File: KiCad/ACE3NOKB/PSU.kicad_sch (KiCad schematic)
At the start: 34 parts, among them U301 74AHCT1G08

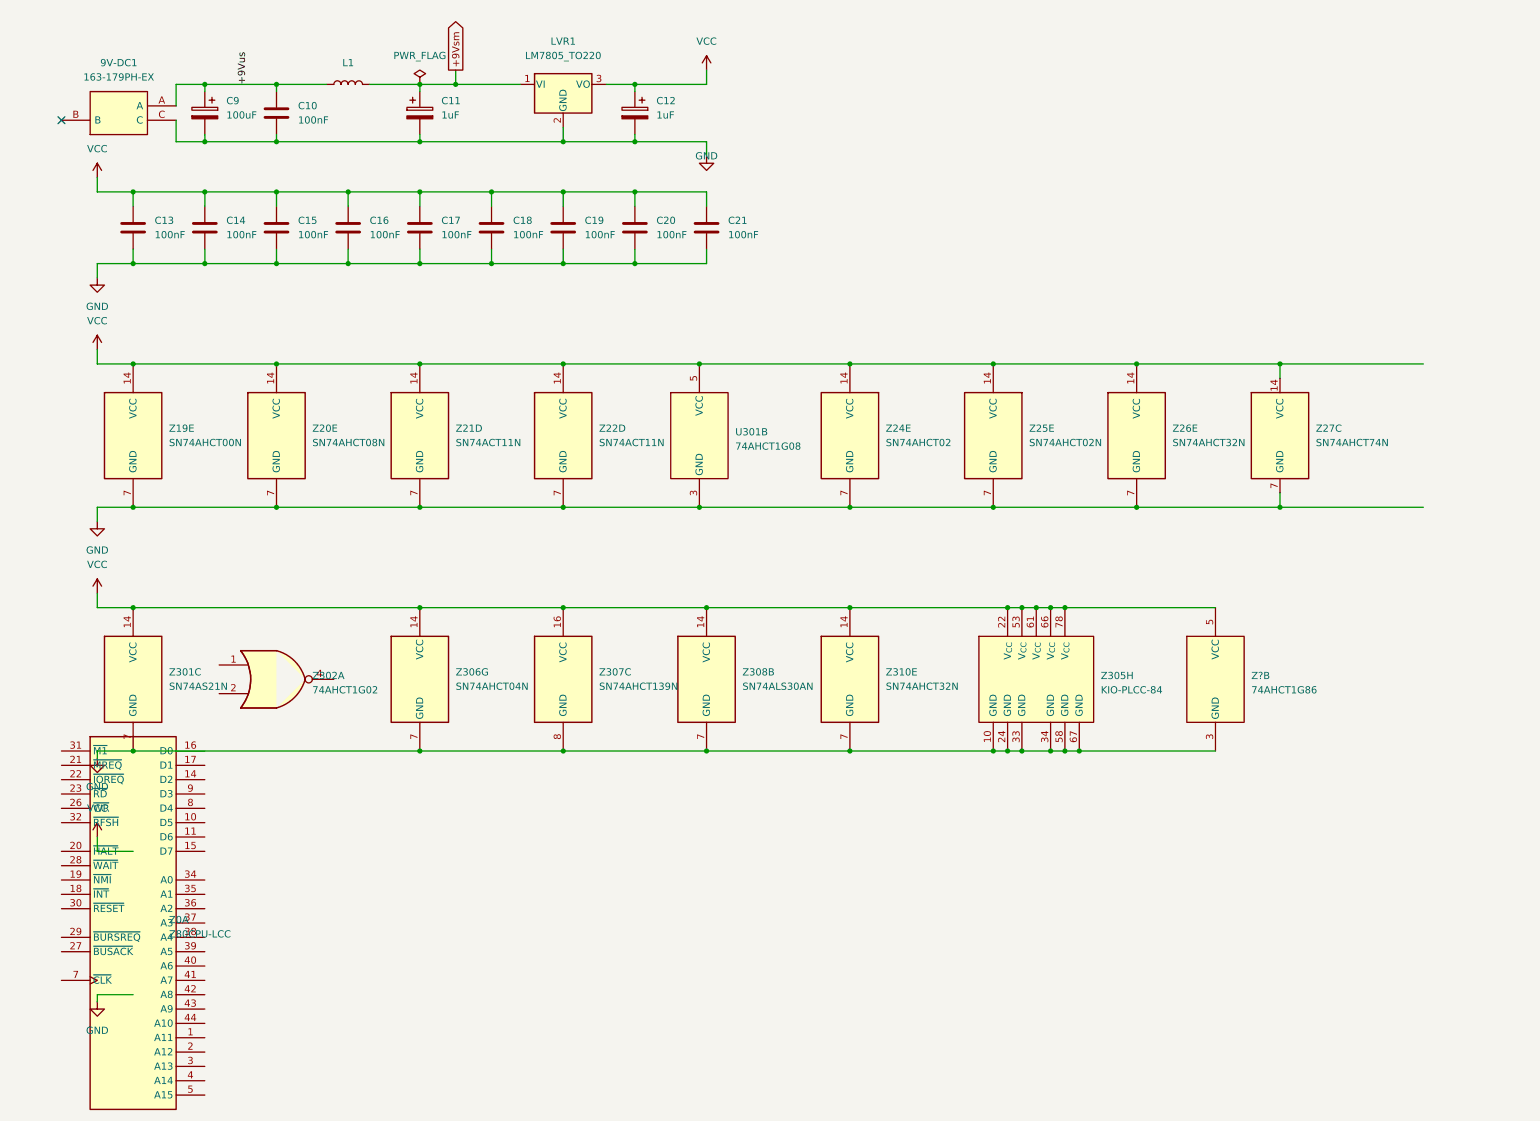
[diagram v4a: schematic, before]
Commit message: Some surface mounted devices and 1G gates for space. Switch able bwteen speeds and witha Freuqency Multiplier to augment the orginal crystal.
Signed-off-by: John Bradley <flypie@rocketmail.com>
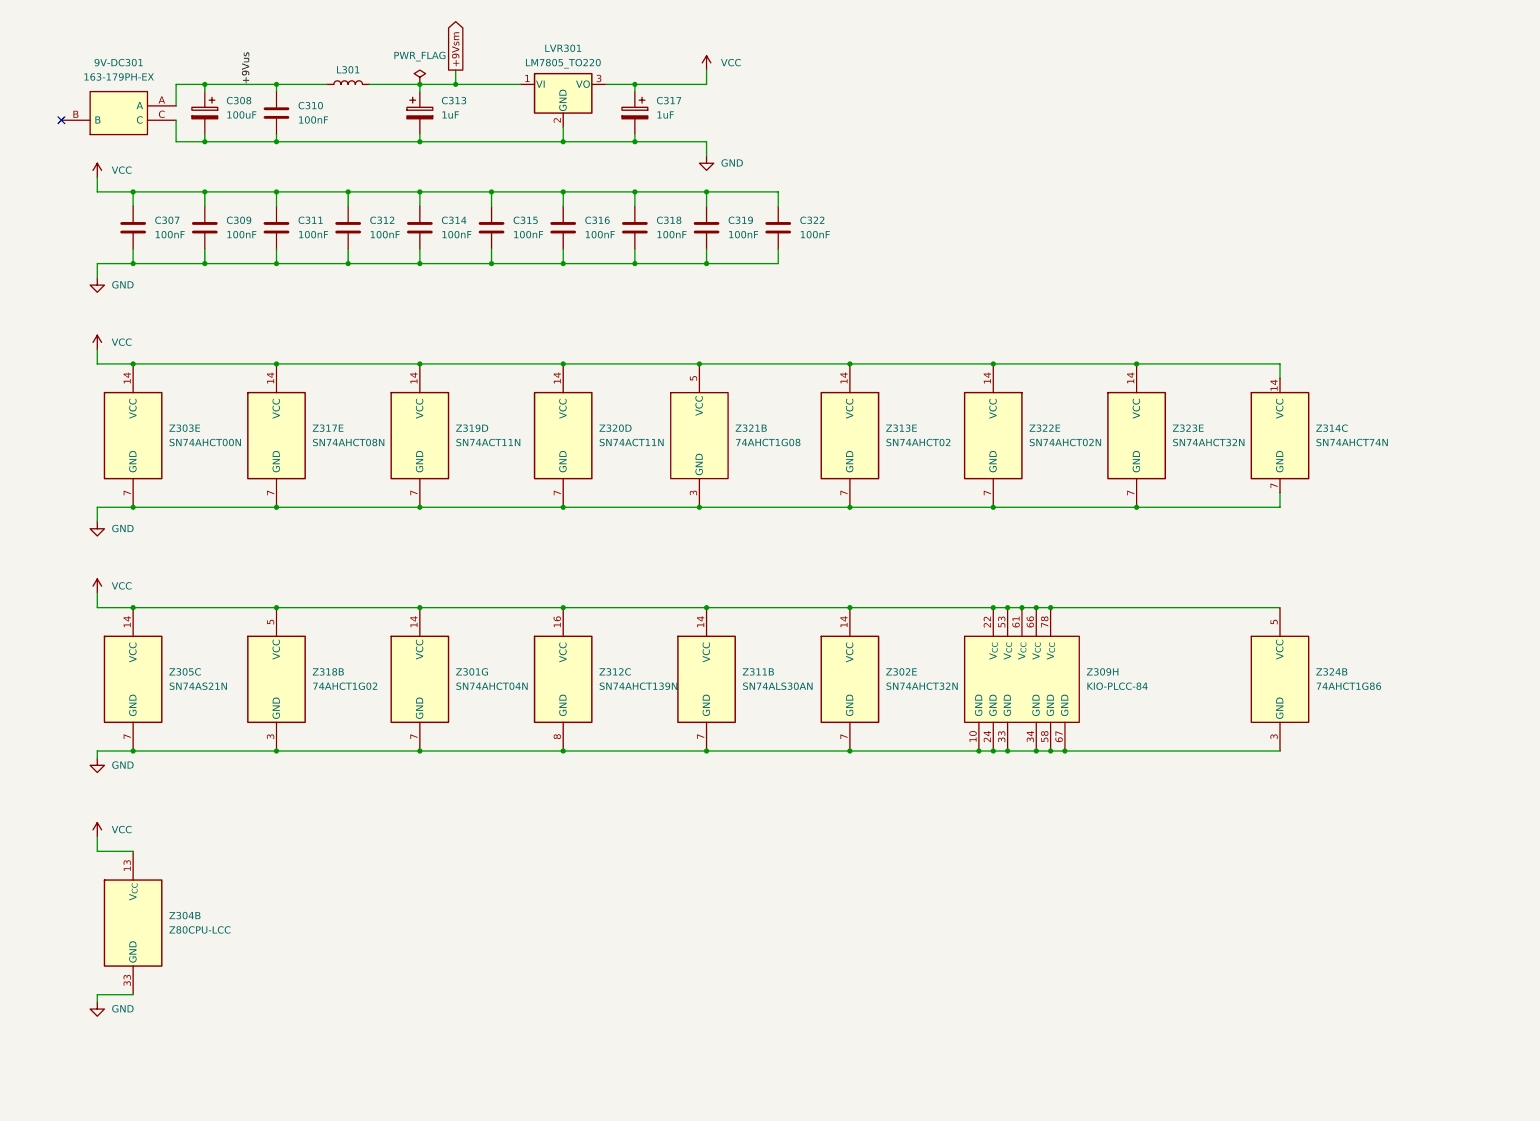
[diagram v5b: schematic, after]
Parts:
- added C322: 100nF, Capacitor_SMD:C_0805_2012Metric, symbol Device:C
- C307: renamed from C13; footprint Capacitor_THT:C_Disc_D3.0mm_W1.6mm_P2.50mm -> Capacitor_THT:C_Rect_L7.0mm_W2.0mm_P5.00mm
- C308: renamed from C9; Manufacturer_Name (none) -> SR PASSIVES; Manufacturer_Part_Number (none) -> CT40805B104K500F3R
- C309: renamed from C14; footprint Capacitor_THT:C_Disc_D3.0mm_W1.6mm_P2.50mm -> Capacitor_THT:C_Rect_L7.0mm_W2.0mm_P5.00mm
- C310: renamed from C10; footprint Capacitor_THT:C_Disc_D3.0mm_W1.6mm_P2.50mm -> Capacitor_THT:C_Rect_L7.0mm_W2.0mm_P5.00mm
- C311: renamed from C15; footprint Capacitor_THT:C_Disc_D3.0mm_W1.6mm_P2.50mm -> Capacitor_THT:C_Rect_L7.0mm_W2.0mm_P5.00mm
- C312: renamed from C16; footprint Capacitor_THT:C_Disc_D3.0mm_W1.6mm_P2.50mm -> Capacitor_THT:C_Rect_L7.0mm_W2.0mm_P5.00mm
- C314: renamed from C17; footprint Capacitor_THT:C_Disc_D3.0mm_W1.6mm_P2.50mm -> Capacitor_THT:C_Rect_L7.0mm_W2.0mm_P5.00mm
- C315: renamed from C18; footprint Capacitor_THT:C_Disc_D3.0mm_W1.6mm_P2.50mm -> Capacitor_THT:C_Rect_L7.0mm_W2.0mm_P5.00mm
- C316: renamed from C19; footprint Capacitor_THT:C_Disc_D3.0mm_W1.6mm_P2.50mm -> Capacitor_THT:C_Rect_L7.0mm_W2.0mm_P5.00mm
- C318: renamed from C20; footprint Capacitor_THT:C_Disc_D3.0mm_W1.6mm_P2.50mm -> Capacitor_THT:C_Rect_L7.0mm_W2.0mm_P5.00mm
- C319: renamed from C21; footprint Capacitor_THT:C_Disc_D3.0mm_W1.6mm_P2.50mm -> Capacitor_THT:C_Rect_L7.0mm_W2.0mm_P5.00mm
- gave numbers to parts that had none: 1
- renumbered 9V-DC1 to 9V-DC301, C11 to C313, C12 to C317, L1 to L301, LVR1 to LVR301, Z306 to Z301, Z310 to Z302, Z19 to Z303, Z0 to Z304, Z301 to Z305, Z305 to Z309, Z308 to Z311, Z307 to Z312, Z24 to Z313, Z27 to Z314, Z20 to Z317, Z302 to Z318, Z21 to Z319, Z22 to Z320, U301 to Z321, Z25 to Z322, Z26 to Z323
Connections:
- net GND: now also Z304.33 (GND), Z318.3 (GND), C322.1
- net VCC: now also Z304.13 (V_{CC}), Z318.5 (VCC), C322.2
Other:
- moved on the sheet: Z309H, Z324B

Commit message: Update, with new Clock Multiplier and Wait functionality.
Signed-off-by: John Bradley <flypie@rocketmail.com>
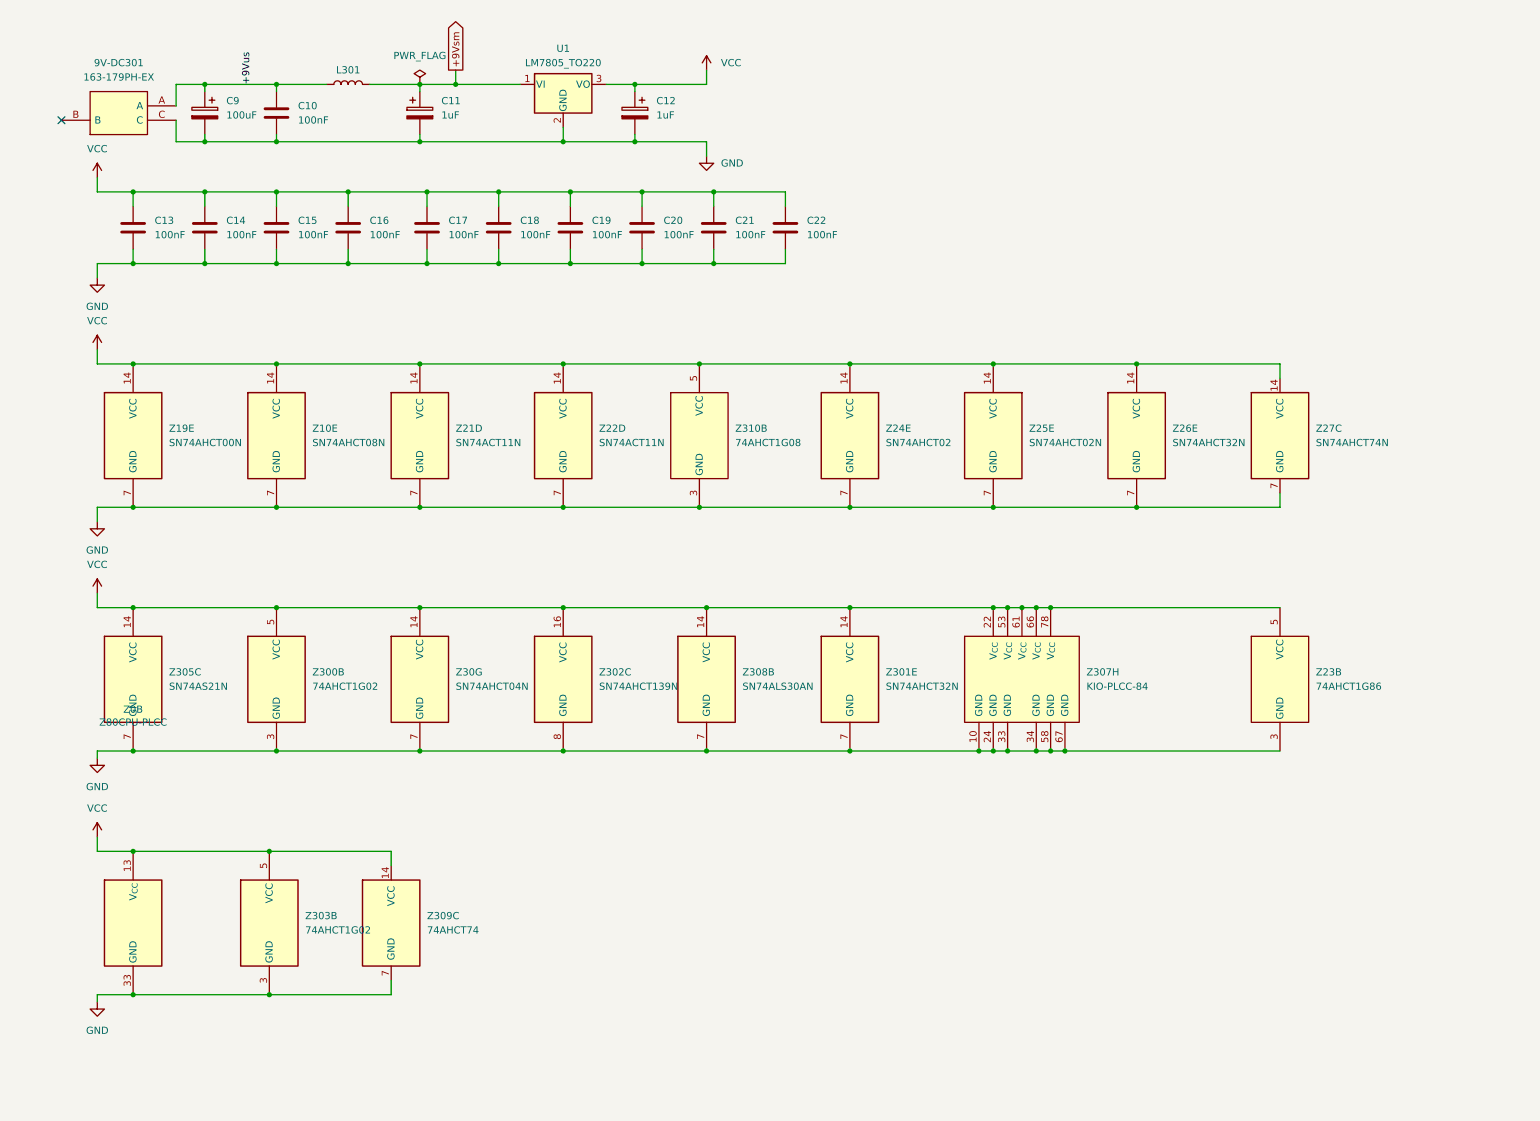
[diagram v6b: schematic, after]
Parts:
- removed C307: 100nF, Capacitor_THT:C_Rect_L7.0mm_W2.0mm_P5.00mm, symbol Device:C
- added C21: 100nF, Capacitor_THT:C_Disc_D4.3mm_W1.9mm_P5.00mm, symbol Device:C
- added Z303: 74AHCT1G02, Package_TO_SOT_SMD:SOT-23-5_HandSoldering, symbol MY74xGxx:74AHCT1G02
- added Z309: 74AHCT74, Package_SO:SOIC-14_3.9x8.7mm_P1.27mm, symbol 74xx-FIX:74LS74
- 9V-DC301: value 163-179PH-EX -> 163-179PH-EX
- C10: renamed from C310; footprint Capacitor_THT:C_Rect_L7.0mm_W2.0mm_P5.00mm -> Capacitor_THT:C_Disc_D4.3mm_W1.9mm_P5.00mm
- C13: renamed from C309; footprint Capacitor_THT:C_Rect_L7.0mm_W2.0mm_P5.00mm -> Capacitor_THT:C_Disc_D4.3mm_W1.9mm_P5.00mm
- C14: renamed from C311; footprint Capacitor_THT:C_Rect_L7.0mm_W2.0mm_P5.00mm -> Capacitor_THT:C_Disc_D4.3mm_W1.9mm_P5.00mm
- C15: renamed from C312; footprint Capacitor_THT:C_Rect_L7.0mm_W2.0mm_P5.00mm -> Capacitor_THT:C_Disc_D4.3mm_W1.9mm_P5.00mm
- C16: renamed from C314; footprint Capacitor_THT:C_Rect_L7.0mm_W2.0mm_P5.00mm -> Capacitor_THT:C_Disc_D4.3mm_W1.9mm_P5.00mm
- C17: renamed from C316; footprint Capacitor_THT:C_Rect_L7.0mm_W2.0mm_P5.00mm -> Capacitor_THT:C_Disc_D4.3mm_W1.9mm_P5.00mm
- C18: renamed from C318; footprint Capacitor_THT:C_Rect_L7.0mm_W2.0mm_P5.00mm -> Capacitor_THT:C_Disc_D4.3mm_W1.9mm_P5.00mm
- C19: renamed from C319; footprint Capacitor_THT:C_Rect_L7.0mm_W2.0mm_P5.00mm -> Capacitor_THT:C_Disc_D4.3mm_W1.9mm_P5.00mm
- C22: renamed from C315; footprint Capacitor_THT:C_Rect_L7.0mm_W2.0mm_P5.00mm -> Capacitor_THT:C_Disc_D4.3mm_W1.9mm_P5.00mm
- U1: renamed from LVR301; footprint Package_TO_SOT_THT:TO-220-3_Horizontal_TabDown -> ExtraFootprints:TO-220-3_Horizontal_TabDown_HS
- Z0: renamed from Z304; value Z80CPU-LCC -> Z80CPU-PLCC
- Z10: renamed from Z317; symbol 74xx:74LS08 -> 74xx-FIX:74LS08
- Z19: renamed from Z303; symbol 74xx:74LS00 -> 74xx-FIX:74LS00
- Z21: renamed from Z319; symbol 74xx:74LS11 -> 74xx-FIX:74LS11
- Z22: renamed from Z320; symbol 74xx:74LS11 -> 74xx-FIX:74LS11
- Z23: renamed from Z324; symbol 74xGxx:74AHCT1G86 -> MY74xGxx:74AHCT1G86
- Z24: renamed from Z313; symbol 74xx:74LS02 -> 74xx-FIX:74LS02
- Z25: renamed from Z322; symbol 74xx:74LS02 -> 74xx-FIX:74LS02
- Z26: renamed from Z323; symbol 74xx:74LS32 -> 74xx-FIX:74LS32
- Z300: renamed from Z318; symbol 74xGxx:74AHCT1G02 -> MY74xGxx:74AHCT1G02
- Z301: renamed from Z302; symbol 74xx:74LS32 -> 74xx-FIX:74LS32
- Z302: renamed from Z312; value SN74AHCT139N -> SN74AHCT139N
- Z308: renamed from Z311; value SN74ALS30AN -> SN74ALS30AN
- Z310: renamed from Z321; symbol 74xGxx:74AHCT1G08 -> MY74xGxx:74AHCT1G08
- renumbered C313 to C11, C317 to C12, C322 to C20, C308 to C9, Z314 to Z27, Z301 to Z30, Z309 to Z307
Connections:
- net GND: now also C21.1, Z303.3 (GND), Z309.7 (GND)
- net VCC: now also C21.2, Z303.5 (VCC), Z309.14 (VCC)
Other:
- moved on the sheet: C13, C14, C15, C16, C17, C18, C19, C20, C22
